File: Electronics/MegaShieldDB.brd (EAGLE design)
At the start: 99.8 x 80 mm, 44 parts, among them IC1 4013N, IC2 MCP4802, IC3 MCP4802, Q1 TIP3055, Q2 TIP3055, X1 Panel, X2 Cruise, X3 Motor, X4 Steer, X5 Brake

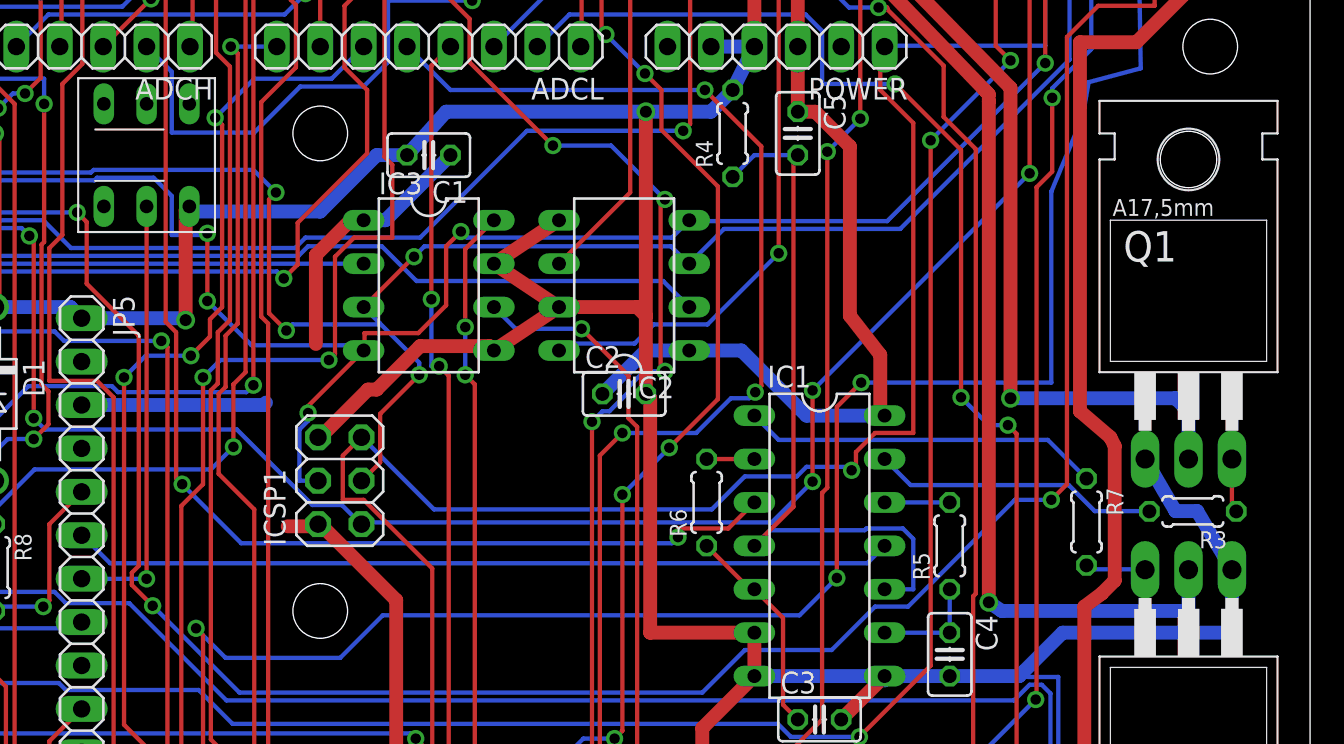
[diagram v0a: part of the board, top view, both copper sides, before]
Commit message: Corrected Base/Emitteron Q1, Q2
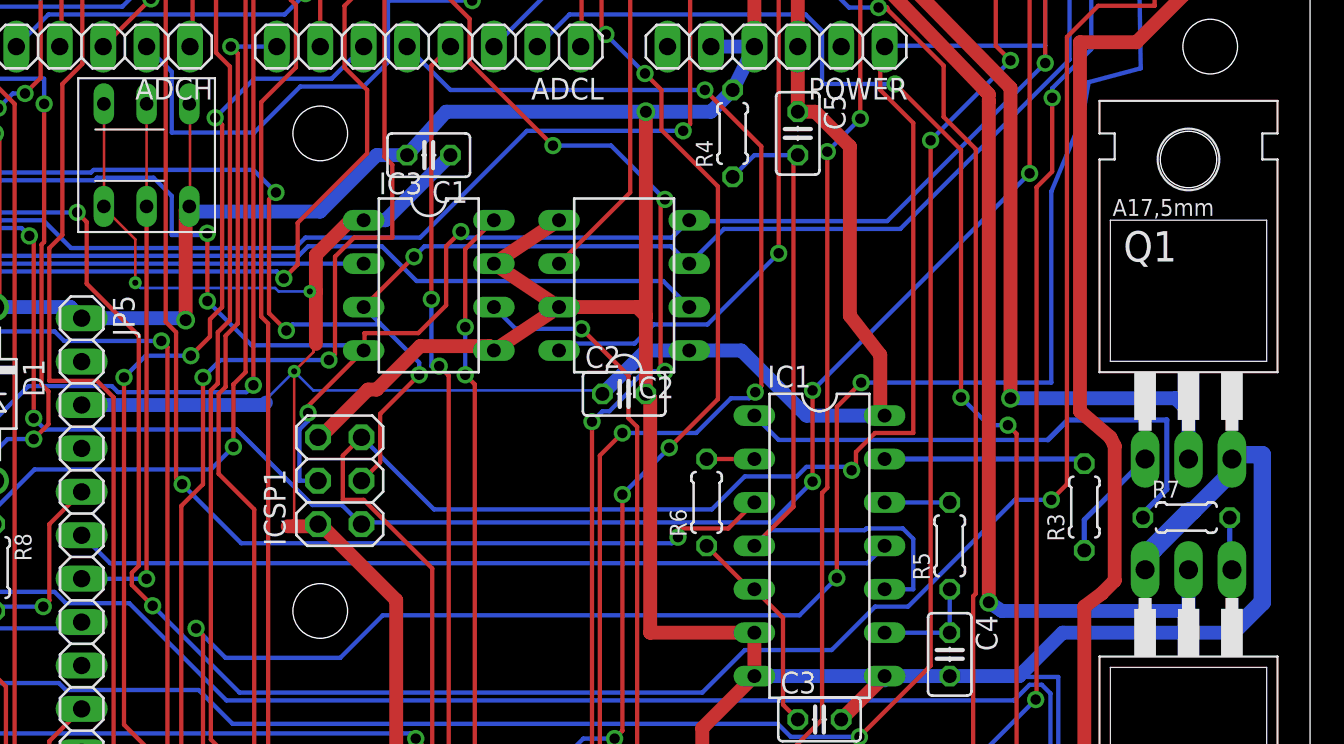
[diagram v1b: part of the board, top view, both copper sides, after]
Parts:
- moved R3 6.36 mm to (86.6, 34.0), turned to 90 degrees
- moved R7 5.85 mm to (92.6, 33.4), turned to 0 degrees
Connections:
- net GND: now also Q1.3, Q2.3; no longer Q1.1, Q2.1
- net N$3: now also Q2.1; no longer Q2.3
- net N$33: now also Q1.1; no longer Q1.3
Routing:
- net +5V: track 203.5 -> 257.7 mm, vias 6 -> 9
- net GND: track 395.4 -> 415.3 mm
- net N$2: track 21.0 -> 31.8 mm
- net N$28: track 25.6 -> 31.6 mm
- net N$4: track 16.8 -> 11.8 mm
- net N$33: track 3.18 -> 6.82 mm
